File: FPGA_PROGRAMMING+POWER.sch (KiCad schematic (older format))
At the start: 28 parts, among them U301 iCE40-HX4K-TQ144, U302 25LC_EEPROM

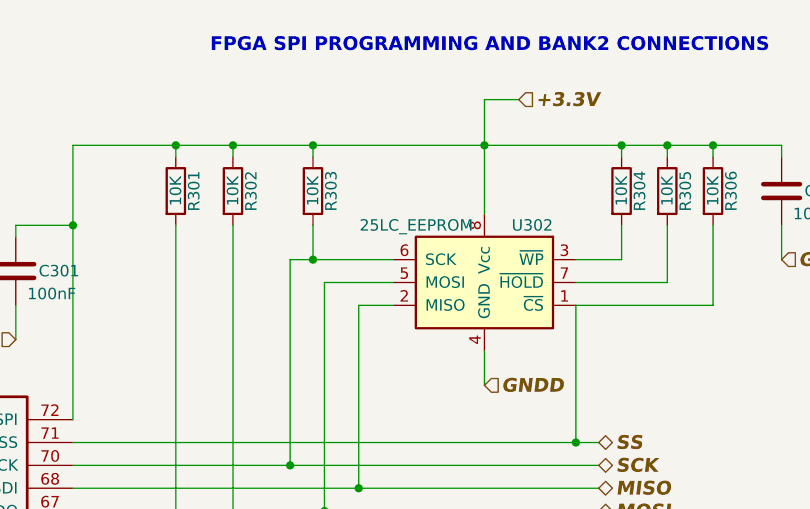
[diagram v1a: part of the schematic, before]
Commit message: Updated MPN to components avalaible in mouser. Updating footprints now ...
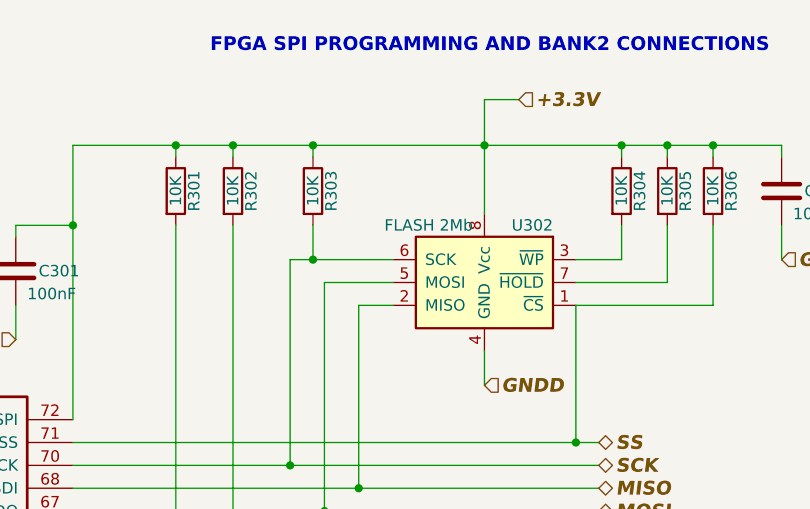
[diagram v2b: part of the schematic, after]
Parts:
- C303, C306: MPN GRM188R61C105KA93D -> C0603C105K8PACTU; VDC 16V -> 10V
- U302: value 25LC_EEPROM -> FLASH 2Mb; MPN 25LC_EEPROM -> LE25U20AMB-AH

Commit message: Updated some footprints. Not updated audio jack and BNC.
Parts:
- U302: footprint TO_SOT_Packages_SMD:SOT-23-8_Handsoldering -> Housings_SOIC:SOIC-8_3.9x4.9mm_Pitch1.27mm
